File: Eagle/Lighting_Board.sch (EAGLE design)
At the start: 15 parts

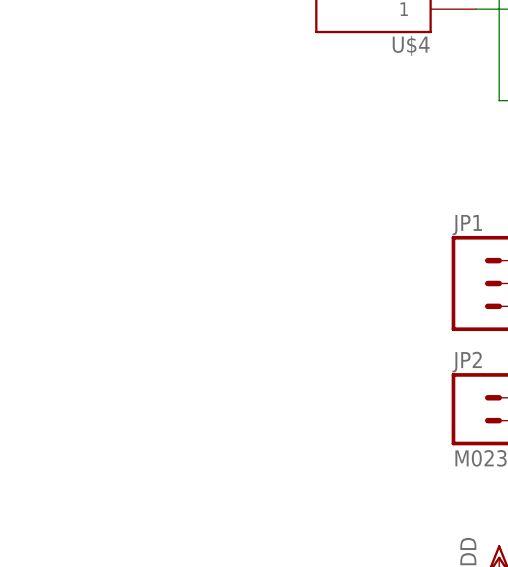
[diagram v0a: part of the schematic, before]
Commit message: Added mounting holes
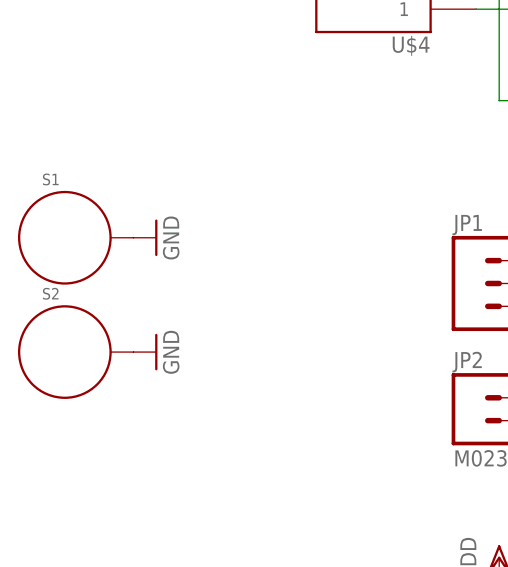
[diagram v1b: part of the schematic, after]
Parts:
- added S1, S2: STANDOFF_ELECTRICAL, SparkFun-Electromechanical:STANDOFF_ELECTRICAL
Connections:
- net GND: now also S1.P$1, S2.P$1
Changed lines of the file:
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@@
 <part name="VDD3" library="supply1" deviceset="VDD" device=""/>
 <part name="VDD4" library="supply1" deviceset="VDD" device=""/>
+<part name="S1" library="SparkFun-Electromechanical" deviceset="STANDOFF_ELECTRICAL" device=""/>
+<part name="GND9" library="SparkFun-Aesthetics" deviceset="GND" device=""/>
+<part name="S2" library="SparkFun-Electromechanical" deviceset="STANDOFF_ELECTRICAL" device=""/>
+<part name="GND10" library="SparkFun-Aesthetics" deviceset="GND" device=""/>
 </parts>
 <sheets>
@@
 <instance part="VDD3" gate="G$1" x="-12.7" y="-27.94"/>
 <instance part="VDD4" gate="G$1" x="-20.32" y="-27.94"/>
+<instance part="S1" gate="G$1" x="-68.58" y="7.62"/>
+<instance part="GND9" gate="1" x="-58.42" y="7.62" rot="R90"/>
+<instance part="S2" gate="G$1" x="-68.58" y="-5.08"/>
+<instance part="GND10" gate="1" x="-58.42" y="-5.08" rot="R90"/>
 </instances>
 <busses>
@@
 <pinref part="GND8" gate="1" pin="GND"/>
 </segment>
+<segment>
+<pinref part="S1" gate="G$1" pin="P$1"/>
+<pinref part="GND9" gate="1" pin="GND"/>
+</segment>
+<segment>
+<pinref part="S2" gate="G$1" pin="P$1"/>
+<pinref part="GND10" gate="1" pin="GND"/>
+</segment>
 </net>
